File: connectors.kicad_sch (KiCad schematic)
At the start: 23 parts, among them J2 SM08B-SRSS-TB

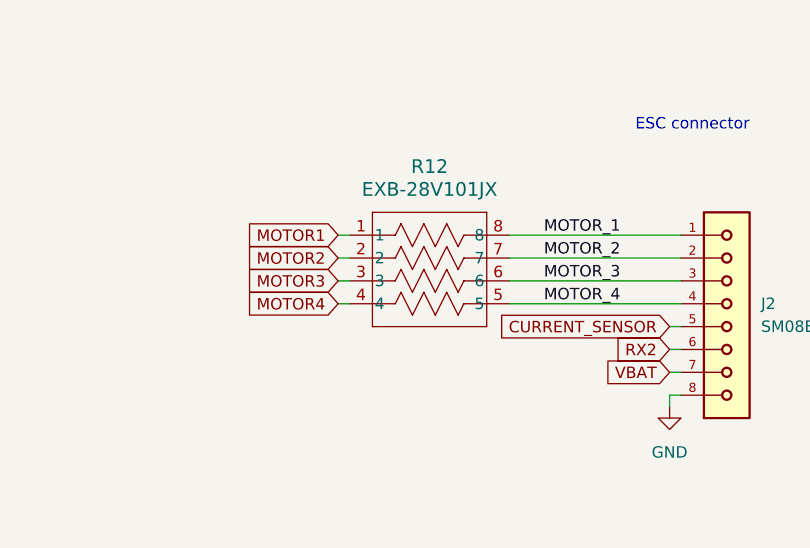
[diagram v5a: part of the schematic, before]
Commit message: add additional wire connections and update MOTOR labels in schematic
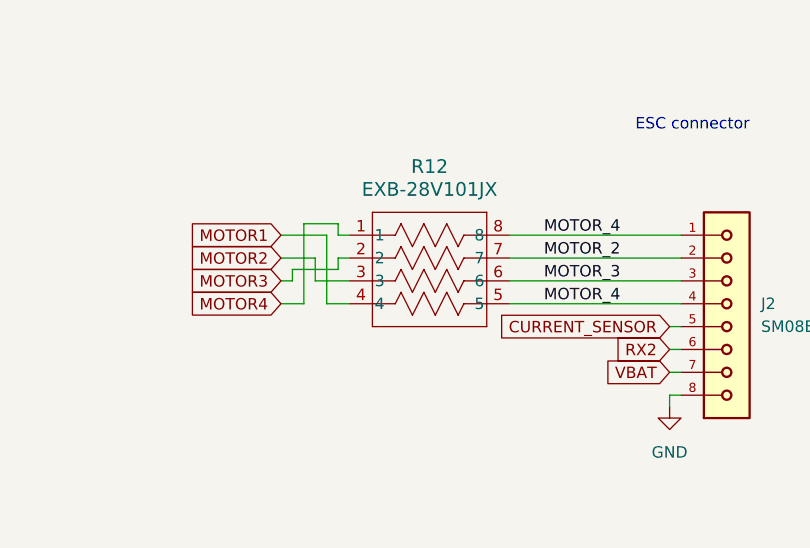
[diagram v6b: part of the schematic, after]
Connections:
- net MOTOR_1 is gone; now on net MOTOR_4: J2.1, R12.8
- net MOTOR1: now also R12.4; no longer R12.1
- net MOTOR2: now also R12.3; no longer R12.2
- net MOTOR3: now also R12.2; no longer R12.3
- net MOTOR4: now also R12.1; no longer R12.4
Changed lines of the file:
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@@
+	(wire
+		(pts
+			(xy 191.77 36.83) (xy 193.04 36.83)
+		)
+		(stroke
+			(width 0)
+			(type default)
+		)
+	)
+	(wire
+		(pts
+			(xy 185.42 44.45) (xy 187.96 44.45)
+		)
+		(stroke
+			(width 0)
+			(type default)
+		)
+	)
 	(wire
 		(pts
@@
 	(wire
 		(pts
+			(xy 189.23 41.91) (xy 193.04 41.91)
+		)
+		(stroke
+			(width 0)
+			(type default)
+		)
+	)
+	(wire
+		(pts
 			(xy 95.25 31.75) (xy 96.52 31.75)
 		)
@@
 	(wire
 		(pts
+			(xy 189.23 39.37) (xy 189.23 41.91)
+		)
+		(stroke
+			(width 0)
+			(type default)
+		)
+	)
+	(wire
+		(pts
 			(xy 228.6 49.53) (xy 229.87 49.53)
 		)
@@
 	(wire
 		(pts
+			(xy 191.77 39.37) (xy 193.04 39.37)
+		)
+		(stroke
+			(width 0)
+			(type default)
+		)
+	)
+	(wire
+		(pts
 			(xy 33.02 35.56) (xy 34.29 35.56)
 		)
@@
 	(wire
 		(pts
-			(xy 191.77 36.83) (xy 193.04 36.83)
-		)
-		(stroke
-			(width 0)
-			(type default)
-		)
-	)
-	(wire
-		(pts
 			(xy 210.82 36.83) (xy 229.87 36.83)
 		)
@@
 	(wire
 		(pts
+			(xy 191.77 40.64) (xy 191.77 39.37)
+		)
+		(stroke
+			(width 0)
+			(type default)
+		)
+	)
+	(wire
+		(pts
 			(xy 228.6 46.99) (xy 229.87 46.99)
 		)
@@
 	(wire
 		(pts
-			(xy 191.77 44.45) (xy 193.04 44.45)
+			(xy 185.42 41.91) (xy 186.69 41.91)
 		)
 		(stroke
@@
 	(wire
 		(pts
+			(xy 186.69 40.64) (xy 191.77 40.64)
+		)
+		(stroke
+			(width 0)
+			(type default)
+		)
+	)
+	(wire
+		(pts
+			(xy 186.69 41.91) (xy 186.69 40.64)
+		)
+		(stroke
+			(width 0)
+			(type default)
+		)
+	)
+	(wire
+		(pts
+			(xy 191.77 35.56) (xy 191.77 36.83)
+		)
+		(stroke
+			(width 0)
+			(type default)
+		)
+	)
+	(wire
+		(pts
+			(xy 190.5 44.45) (xy 193.04 44.45)
+		)
+		(stroke
+			(width 0)
+			(type default)
+		)
+	)
+	(wire
+		(pts
 			(xy 34.29 139.7) (xy 34.29 138.43)
 		)
@@
 	(wire
 		(pts
-			(xy 191.77 41.91) (xy 193.04 41.91)
-		)
-		(stroke
-			(width 0)
-			(type default)
-		)
-	)
-	(wire
-		(pts
 			(xy 96.52 62.23) (xy 97.79 62.23)
 		)
@@
 	(wire
 		(pts
-			(xy 191.77 39.37) (xy 193.04 39.37)
-		)
-		(stroke
-			(width 0)
-			(type default)
-		)
-	)
-	(wire
-		(pts
 			(xy 16.51 118.11) (xy 16.51 138.43)
 		)
@@
 	(wire
 		(pts
+			(xy 185.42 36.83) (xy 190.5 36.83)
+		)
+		(stroke
+			(width 0)
+			(type default)
+		)
+	)
+	(wire
+		(pts
 			(xy 34.29 133.35) (xy 35.56 133.35)
 		)
@@
 	(wire
 		(pts
+			(xy 187.96 35.56) (xy 191.77 35.56)
+		)
+		(stroke
+			(width 0)
+			(type default)
+		)
+	)
+	(wire
+		(pts
+			(xy 190.5 36.83) (xy 190.5 44.45)
+		)
+		(stroke
+			(width 0)
+			(type default)
+		)
+	)
+	(wire
+		(pts
+			(xy 187.96 44.45) (xy 187.96 35.56)
+		)
+		(stroke
+			(width 0)
+			(type default)
+		)
+	)
+	(wire
+		(pts
 			(xy 228.6 55.88) (xy 228.6 54.61)
 		)
@@
 		(pts
 			(xy 96.52 63.5) (xy 96.52 62.23)
+		)
+		(stroke
+			(width 0)
+			(type default)
+		)
+	)
+	(wire
+		(pts
+			(xy 185.42 39.37) (xy 189.23 39.37)
 		)
 		(stroke
@@
 		)
 	)
-	(label "MOTOR_1"
+	(label "MOTOR_4"
 		(at 214.63 36.83 0)
 		(effects
@@
 	(global_label "MOTOR1"
 		(shape input)
-		(at 191.77 36.83 180)
-		(fields_autoplaced yes)
-		(effects
-			(font
-				(size 1.27 1.27)
-			)
-			(justify right)
-		)
-		(property "Intersheetrefs" "${INTERSHEET_REFS}"
-			(at 181.2253 36.83 0)
+		(at 185.42 36.83 180)
+		(fields_autoplaced yes)
+		(effects
+			(font
+				(size 1.27 1.27)
+			)
+			(justify right)
+		)
+		(property "Intersheetrefs" "${INTERSHEET_REFS}"
+			(at 174.8753 36.83 0)
 			(effects
 				(font
@@
 	(global_label "MOTOR3"
 		(shape input)
-		(at 191.77 41.91 180)
-		(fields_autoplaced yes)
-		(effects
-			(font
-				(size 1.27 1.27)
-			)
-			(justify right)
-		)
-		(property "Intersheetrefs" "${INTERSHEET_REFS}"
-			(at 181.2253 41.91 0)
+		(at 185.42 41.91 180)
+		(fields_autoplaced yes)
+		(effects
+			(font
+				(size 1.27 1.27)
+			)
+			(justify right)
+		)
+		(property "Intersheetrefs" "${INTERSHEET_REFS}"
+			(at 174.8753 41.91 0)
 			(effects
 				(font
@@
 	(global_label "MOTOR4"
 		(shape input)
-		(at 191.77 44.45 180)
-		(fields_autoplaced yes)
-		(effects
-			(font
-				(size 1.27 1.27)
-			)
-			(justify right)
-		)
-		(property "Intersheetrefs" "${INTERSHEET_REFS}"
-			(at 181.2253 44.45 0)
+		(at 185.42 44.45 180)
+		(fields_autoplaced yes)
+		(effects
+			(font
+				(size 1.27 1.27)
+			)
+			(justify right)
+		)
+		(property "Intersheetrefs" "${INTERSHEET_REFS}"
+			(at 174.8753 44.45 0)
 			(effects
 				(font
@@
 	(global_label "MOTOR2"
 		(shape input)
-		(at 191.77 39.37 180)
-		(fields_autoplaced yes)
-		(effects
-			(font
-				(size 1.27 1.27)
-			)
-			(justify right)
-		)
-		(property "Intersheetrefs" "${INTERSHEET_REFS}"
-			(at 181.2253 39.37 0)
-			(effects
-				(font
+		(at 185.42 39.37 180)
+		(fields_autoplaced yes)
+		(effects
+			(font
+				(size 1.27 1.27)
+			)
+			(justify right)
+		)
+		(property "Intersheetrefs" "${INTERSHEET_REFS}"
+			(at 174.8753 39.37 0)
+			(effects
+				(font

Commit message: routing...
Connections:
- net MOTOR1: now also R12.8; no longer R12.4
- net MOTOR2: now also R12.7; no longer R12.3
- net MOTOR3: now also R12.6; no longer R12.2
- net MOTOR4: now also R12.5; no longer R12.1
- net MOTOR_2: now also R12.2; no longer R12.7
- net MOTOR_3: now also R12.3; no longer R12.6
- net MOTOR_4: now also R12.4; no longer J2.1, R12.5, R12.8
- new net MOTOR_1: J2.1, R12.1

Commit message: routing...
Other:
- note added: "Refaire footprint de la quadri resistance"
- moved on the sheet: J2, R12, U18, U19, U22, U24, U25
